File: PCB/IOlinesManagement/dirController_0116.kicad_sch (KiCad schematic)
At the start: 49 parts, among them K1 HK19F-DCxxV-SHC, K10 HK19F-DCxxV-SHC, K11 HK19F-DCxxV-SHC, K12 HK19F-DCxxV-SHC, K13 HK19F-DCxxV-SHC, K14 HK19F-DCxxV-SHC, K15 HK19F-DCxxV-SHC, K16 HK19F-DCxxV-SHC, K2 HK19F-DCxxV-SHC, K3 HK19F-DCxxV-SHC, K4 HK19F-DCxxV-SHC, K5 HK19F-DCxxV-SHC, K6 HK19F-DCxxV-SHC, K7 HK19F-DCxxV-SHC, K8 HK19F-DCxxV-SHC, K9 HK19F-DCxxV-SHC, Q1 BC337, Q10 BC337, Q11 BC337, Q12 BC337, Q13 BC337, Q14 BC337, Q15 BC337, Q16 BC337, Q2 BC337, Q3 BC337, Q4 BC337, Q5 BC337, Q6 BC337, Q7 BC337, Q8 BC337, Q9 BC337

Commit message: Duplicated components names fixed
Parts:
- renumbered K5 to K2, K2 to K3, K3 to K4, K4 to K5, Q2 to Q1, Q9 to Q10, Q10 to Q11, Q11 to Q12, Q14 to Q13, Q15 to Q14, Q16 to Q15, Q13 to Q16, Q1 to Q2, Q4 to Q3, Q3 to Q4, Q8 to Q5, Q5 to Q7, Q7 to Q8, Q12 to Q9, R9 to R10, R7 to R2, R2 to R3, R8 to R4, R4 to R7, R3 to R8, R10 to R9

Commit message: Fingerprints assignment
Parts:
- ExtPwr_1: footprint (none) -> Connector_PinHeader_2.54mm:PinHeader_2x09_P2.54mm_Vertical
- Q1, Q10, Q11, Q12, Q13, Q14, Q15, Q16, Q2, Q3, Q4, Q5, Q6, Q7, Q8, Q9: footprint Package_TO_SOT_THT:TO-92_Inline -> Package_TO_SOT_THT:TO-92_Inline_Wide
- R1, R10, R11, R12, R13, R14, R15, R16, R2, R3, R4, R5, R6, R7, R8, R9: footprint (none) -> Resistor_SMD:R_1206_3216Metric
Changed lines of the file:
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@@
 			)
 		)
-		(property "Footprint" "Package_TO_SOT_THT:TO-92_Inline"
+		(property "Footprint" "Package_TO_SOT_THT:TO-92_Inline_Wide"
 			(at 67.056 66.167 0)
 			(effects
@@
 			)
 		)
-		(property "Footprint" "Package_TO_SOT_THT:TO-92_Inline"
+		(property "Footprint" "Package_TO_SOT_THT:TO-92_Inline_Wide"
 			(at 192.278 89.027 0)
 			(effects
@@
 			)
 		)
-		(property "Footprint" "Package_TO_SOT_THT:TO-92_Inline"
+		(property "Footprint" "Package_TO_SOT_THT:TO-92_Inline_Wide"
 			(at 128.016 104.521 0)
 			(effects
@@
 			)
 		)
-		(property "Footprint" "Package_TO_SOT_THT:TO-92_Inline"
+		(property "Footprint" "Package_TO_SOT_THT:TO-92_Inline_Wide"
 			(at 67.056 104.267 0)
 			(effects
@@
 			)
 		)
-		(property "Footprint" "Package_TO_SOT_THT:TO-92_Inline"
+		(property "Footprint" "Package_TO_SOT_THT:TO-92_Inline_Wide"
 			(at 128.524 67.437 0)
 			(effects
@@
 			)
 		)
-		(property "Footprint" "Package_TO_SOT_THT:TO-92_Inline"
+		(property "Footprint" "Package_TO_SOT_THT:TO-92_Inline_Wide"
 			(at 129.032 141.605 0)
 			(effects
@@
 			)
 		)
-		(property "Footprint" ""
+		(property "Footprint" "Resistor_SMD:R_1206_3216Metric"
 			(at 160.528 149.098 90)
 			(effects
@@
 			)
 		)
-		(property "Footprint" "Package_TO_SOT_THT:TO-92_Inline"
+		(property "Footprint" "Package_TO_SOT_THT:TO-92_Inline_Wide"
 			(at 192.278 50.927 0)
 			(effects
@@
 			)
 		)
-		(property "Footprint" ""
+		(property "Footprint" "Resistor_SMD:R_1206_3216Metric"
 			(at 223.774 122.682 90)
 			(effects
@@
 			)
 		)
-		(property "Footprint" "Package_TO_SOT_THT:TO-92_Inline"
+		(property "Footprint" "Package_TO_SOT_THT:TO-92_Inline_Wide"
 			(at 67.31 178.689 0)
 			(effects
@@
 			)
 		)
-		(property "Footprint" "Package_TO_SOT_THT:TO-92_Inline"
+		(property "Footprint" "Package_TO_SOT_THT:TO-92_Inline_Wide"
 			(at 160.401 171.704 0)
 			(effects
@@
 			)
 		)
-		(property "Footprint" "Package_TO_SOT_THT:TO-92_Inline"
+		(property "Footprint" "Package_TO_SOT_THT:TO-92_Inline_Wide"
 			(at 254.254 126.365 0)
 			(effects
@@
 			)
 		)
-		(property "Footprint" ""
+		(property "Footprint" "Resistor_SMD:R_1206_3216Metric"
 			(at 49.53 100.584 90)
 			(effects
@@
 			)
 		)
-		(property "Footprint" ""
+		(property "Footprint" "Resistor_SMD:R_1206_3216Metric"
 			(at 177.038 47.244 90)
 			(effects
@@
 			)
 		)
-		(property "Footprint" ""
+		(property "Footprint" "Resistor_SMD:R_1206_3216Metric"
 			(at 223.774 160.02 90)
 			(effects
@@
 			)
 		)
-		(property "Footprint" "Package_TO_SOT_THT:TO-92_Inline"
+		(property "Footprint" "Package_TO_SOT_THT:TO-92_Inline_Wide"
 			(at 67.31 141.097 0)
 			(effects
@@
 			)
 		)
-		(property "Footprint" ""
+		(property "Footprint" "Resistor_SMD:R_1206_3216Metric"
 			(at 49.784 175.006 90)
 			(effects
@@
 			)
 		)
-		(property "Footprint" ""
+		(property "Footprint" "Resistor_SMD:R_1206_3216Metric"
 			(at 52.324 137.414 90)
 			(effects
@@
 			)
 		)
-		(property "Footprint" ""
+		(property "Footprint" "Resistor_SMD:R_1206_3216Metric"
 			(at 222.504 48.514 90)
 			(effects
@@
 			)
 		)
-		(property "Footprint" "Package_TO_SOT_THT:TO-92_Inline"
+		(property "Footprint" "Package_TO_SOT_THT:TO-92_Inline_Wide"
 			(at 192.532 125.857 0)
 			(effects
@@
 			)
 		)
-		(property "Footprint" "Package_TO_SOT_THT:TO-92_Inline"
+		(property "Footprint" "Package_TO_SOT_THT:TO-92_Inline_Wide"
 			(at 253.238 89.281 0)
 			(effects
@@
 			)
 		)
-		(property "Footprint" "Package_TO_SOT_THT:TO-92_Inline"
+		(property "Footprint" "Package_TO_SOT_THT:TO-92_Inline_Wide"
 			(at 259.207 150.368 0)
 			(effects
@@
 			)
 		)
-		(property "Footprint" ""
+		(property "Footprint" "Resistor_SMD:R_1206_3216Metric"
 			(at 97.282 63.754 90)
 			(effects
@@
 			)
 		)
-		(property "Footprint" "Package_TO_SOT_THT:TO-92_Inline"
+		(property "Footprint" "Package_TO_SOT_THT:TO-92_Inline_Wide"
 			(at 127 178.943 0)
 			(effects
@@
 			)
 		)
-		(property "Footprint" "Package_TO_SOT_THT:TO-92_Inline"
+		(property "Footprint" "Package_TO_SOT_THT:TO-92_Inline_Wide"
 			(at 253.746 52.197 0)
 			(effects
@@
 			)
 		)
-		(property "Footprint" ""
+		(property "Footprint" "Resistor_SMD:R_1206_3216Metric"
 			(at 225.044 85.598 90)
 			(effects
@@
 			)
 		)
-		(property "Footprint" ""
+		(property "Footprint" "Resistor_SMD:R_1206_3216Metric"
 			(at 174.752 85.344 90)
 			(effects
@@
 			)
 		)
-		(property "Footprint" ""
+		(property "Footprint" "Connector_PinHeader_2.54mm:PinHeader_2x09_P2.54mm_Vertical"
 			(at 23.114 19.558 0)
 			(effects
@@
 			)
 		)
-		(property "Footprint" ""
+		(property "Footprint" "Resistor_SMD:R_1206_3216Metric"
 			(at 177.546 122.174 90)
 			(effects
@@
 			)
 		)
-		(property "Footprint" ""
+		(property "Footprint" "Resistor_SMD:R_1206_3216Metric"
 			(at 51.816 62.484 90)
 			(effects
@@
 			)
 		)
-		(property "Footprint" ""
+		(property "Footprint" "Resistor_SMD:R_1206_3216Metric"
 			(at 98.552 175.26 90)
 			(effects
@@
 			)
 		)
-		(property "Footprint" ""
+		(property "Footprint" "Resistor_SMD:R_1206_3216Metric"
 			(at 98.552 137.922 90)
 			(effects
@@
 			)
 		)
-		(property "Footprint" ""
+		(property "Footprint" "Resistor_SMD:R_1206_3216Metric"
 			(at 99.822 100.838 90)
 			(effects

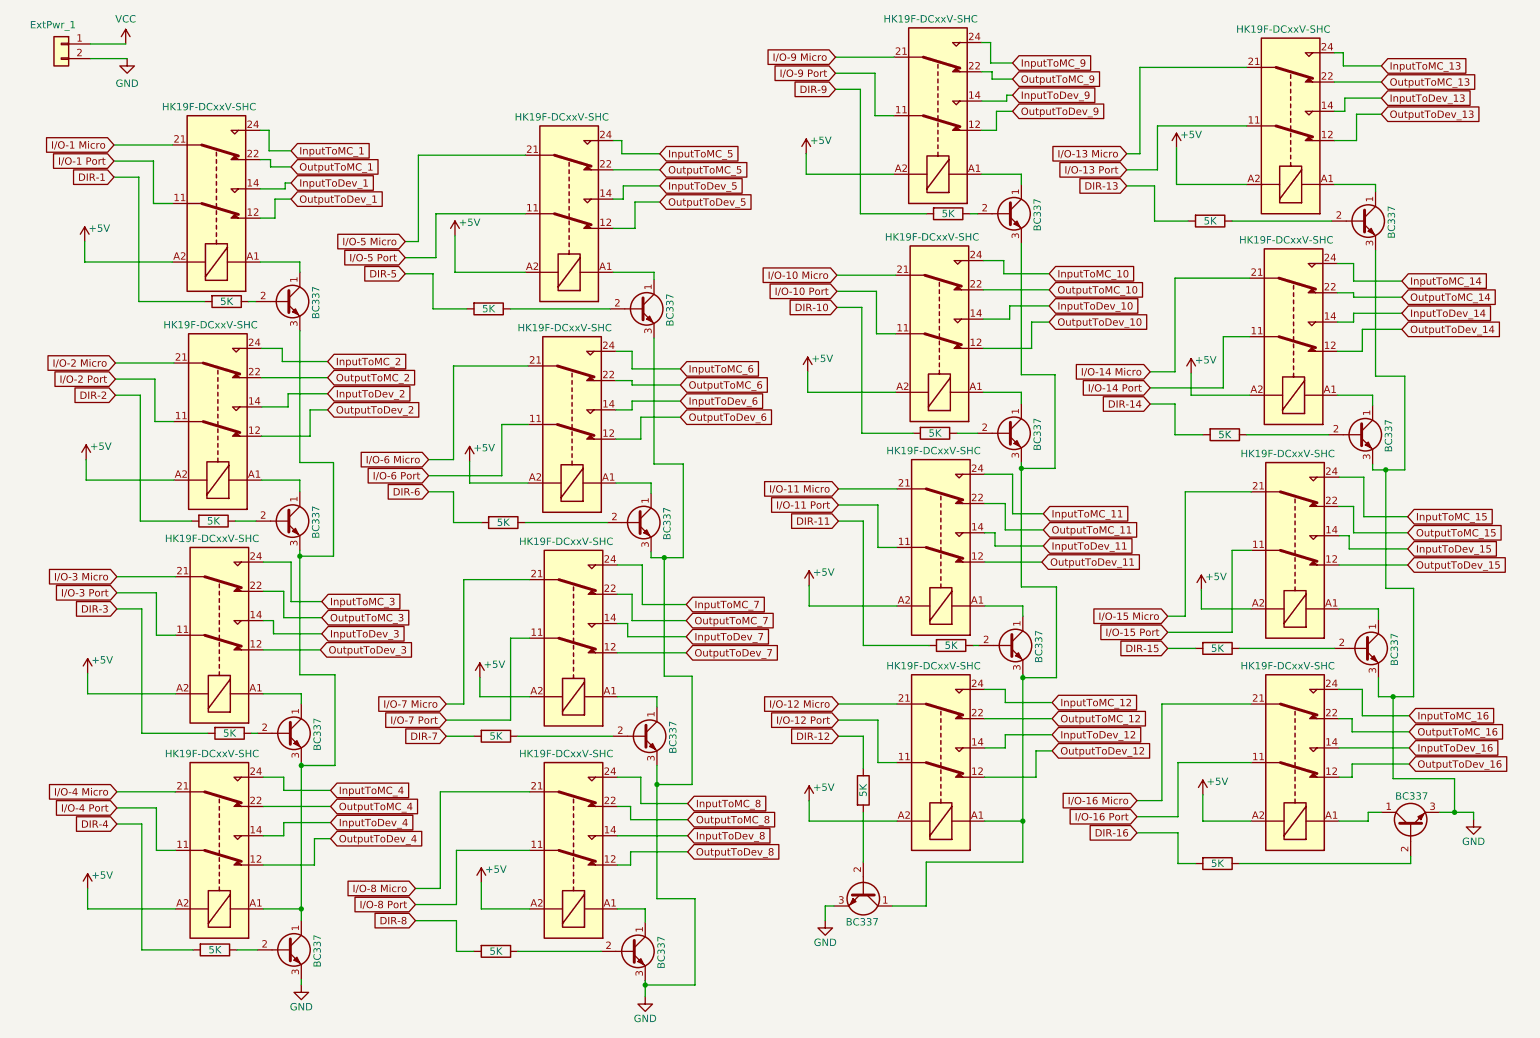
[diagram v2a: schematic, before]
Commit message: Component size reduction and fixes
- Some connection to GND has been fixed
- The biggest part of (THT) BC337 components has been replaced by (SMD) BC817
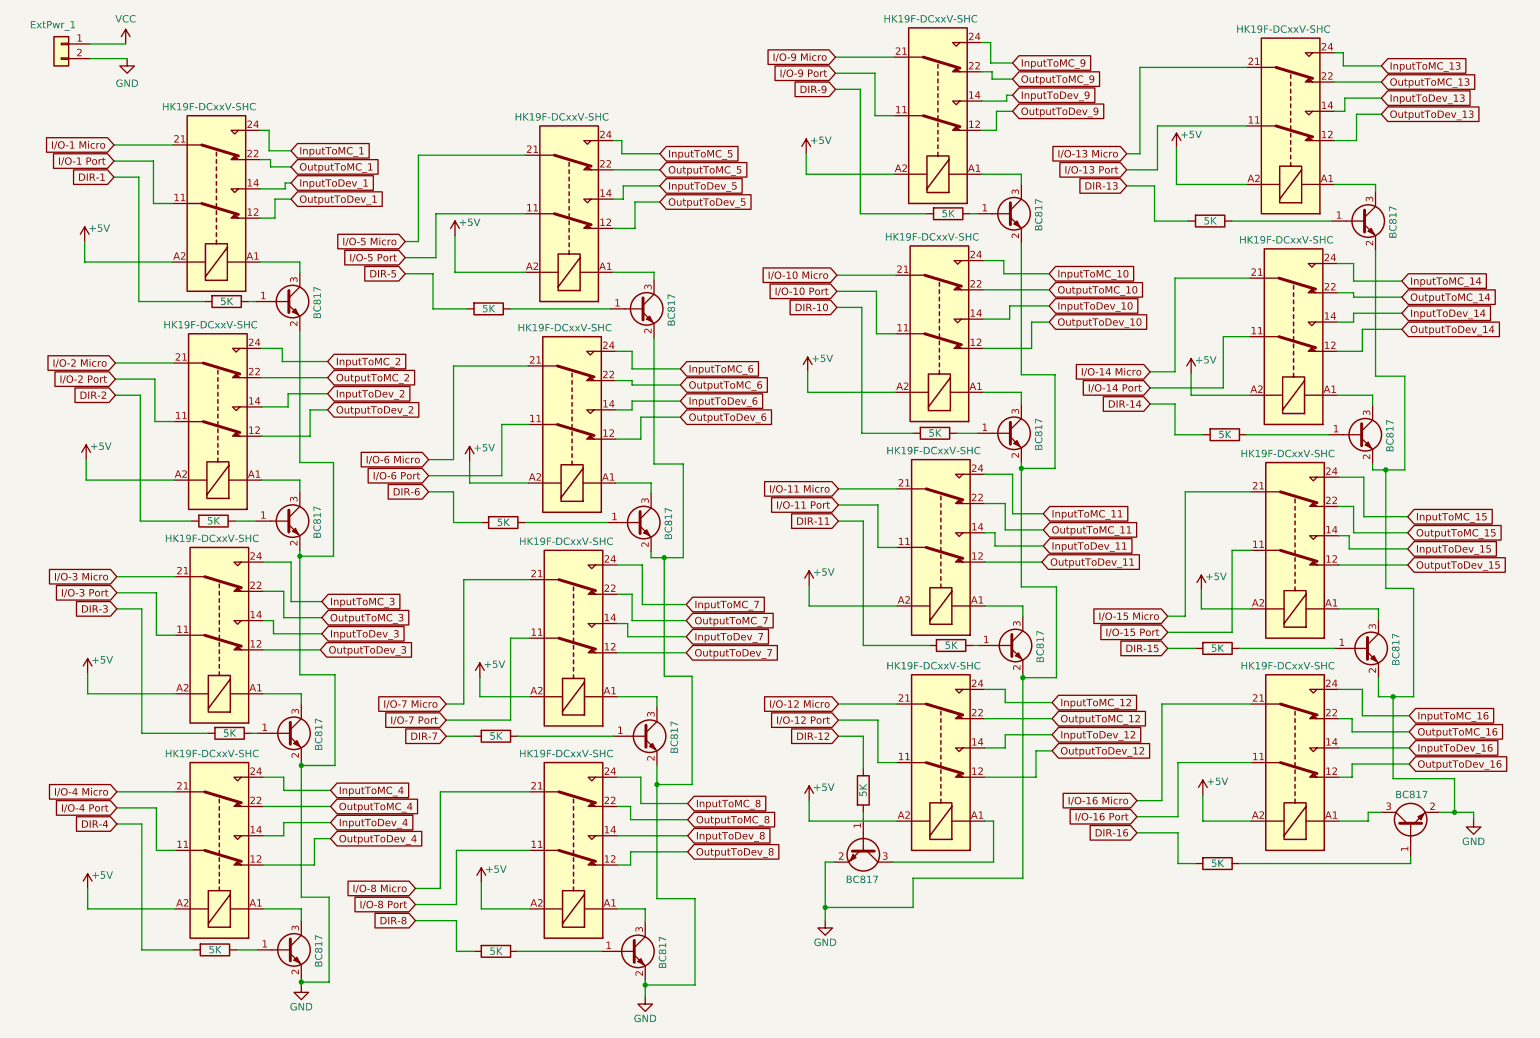
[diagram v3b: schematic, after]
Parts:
- removed Q1, Q10, Q11, Q12, Q13, Q14, Q15, Q16, Q2, Q3, Q4, Q5, Q6, Q7, Q8, Q9: BC337, Package_TO_SOT_THT:TO-92_Inline_Wide, symbol Transistor_BJT:BC337
- added Q1, Q10, Q11, Q12, Q13, Q14, Q15, Q16, Q2, Q3, Q4, Q5, Q6, Q7, Q8, Q9: BC817, Package_TO_SOT_SMD:SOT-23, symbol Transistor_BJT:BC817
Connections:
- net GND: now also Q1.2 (E), Q10.2 (E), Q11.2 (E), Q12.2 (E), Q13.2 (E), Q14.2 (E), Q15.2 (E), Q16.2 (E), Q2.2 (E), Q3.2 (E), Q4.2 (E), Q5.2 (E), Q6.2 (E), Q7.2 (E), Q8.2 (E), Q9.2 (E)
- net at K1.A1: now also Q1.3 (C)
- net at R3.1: now also Q1.1 (B)
- net at K4.A1: now also Q4.3 (C)
- net at K10.A1: now also Q10.3 (C)
- net at R10.1: now also Q10.1 (B)
- net at K12.A1: now also Q12.3 (C)
- net at K6.A1: now also Q6.3 (C)
- net at R8.1: now also Q6.1 (B)
- net at K2.A1: now also Q2.3 (C)
- net at R1.1: now also Q2.1 (B)
- net at K5.A1: now also Q5.3 (C)
- net at R5.1: now also Q5.1 (B)
- net at K16.A1: now also Q13.3 (C)
- net at K7.A1: now also Q7.3 (C)
- net at R6.1: now also Q7.1 (B)
- net at R9.2: now also Q12.1 (B)
- net at K13.A1: now also Q16.3 (C)
- net at K9.A1: now also Q9.3 (C)
- net at R11.1: now also Q9.1 (B)
- net at R14.1: now also Q14.1 (B)
- net at R2.1: now also Q4.1 (B)
- net at K15.A1: now also Q14.3 (C)
- net at R15.1: now also Q13.1 (B)
- net at K14.A1: now also Q15.3 (C)
- net at K8.A1: now also Q8.3 (C)
- net at K3.A1: now also Q3.3 (C)
- net at R4.1: now also Q3.1 (B)
- net at R13.1: now also Q16.1 (B)
- net at K11.A1: now also Q11.3 (C)
- net at R12.1: now also Q11.1 (B)
- net at R16.1: now also Q15.1 (B)
- net at R7.1: now also Q8.1 (B)

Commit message: Fixes
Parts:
- removed ExtPwr_1: Conn_01x02, Connector_PinHeader_2.54mm:PinHeader_2x09_P2.54mm_Vertical, symbol Connector_Generic:Conn_01x02
- renumbered Q9 to Q10, Q10 to Q11, Q11 to Q12, Q15 to Q13, Q16 to Q14, Q14 to Q15, Q13 to Q16, Q8 to Q5, Q5 to Q7, Q7 to Q8, Q12 to Q9
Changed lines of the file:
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@@
 	(wire
 		(pts
-			(xy 28.194 22.098) (xy 34.544 22.098)
-		)
-		(stroke
-			(width 0)
-			(type default)
-		)
-	)
-	(wire
-		(pts
 			(xy 162.306 139.7) (xy 162.306 145.288)
 		)
@@
 	(wire
 		(pts
-			(xy 28.194 19.558) (xy 34.29 19.558)
-		)
-		(stroke
-			(width 0)
-			(type default)
-		)
-	)
-	(wire
-		(pts
 			(xy 121.92 154.178) (xy 121.92 151.892)
 		)
@@
 	)
 	(symbol
-		(lib_id "power:VCC")
-		(at 34.29 19.558 0)
-		(unit 1)
-		(exclude_from_sim no)
-		(in_bom yes)
-		(on_board yes)
-		(dnp no)
-		(fields_autoplaced yes)
-		(property "Reference" "#PWR07"
-			(at 34.29 23.368 0)
-			(effects
-				(font
-					(size 1.27 1.27)
-				)
-				(hide yes)
-			)
-		)
-		(property "Value" "VCC"
-			(at 34.29 15.24 0)
-			(effects
-				(font
-					(size 1.27 1.27)
-				)
-			)
-		)
-		(property "Footprint" ""
-			(at 34.29 19.558 0)
-			(effects
-				(font
-					(size 1.27 1.27)
-				)
-				(hide yes)
-			)
-		)
-		(property "Datasheet" ""
-			(at 34.29 19.558 0)
-			(effects
-				(font
-					(size 1.27 1.27)
-				)
-				(hide yes)
-			)
-		)
-		(property "Description" "Power symbol creates a global label with name \"VCC\""
-			(at 34.29 19.558 0)
-			(effects
-				(font
-					(size 1.27 1.27)
-				)
-				(hide yes)
-			)
-		)
-		(pin "1"
-		)
-		(instances
-			(project ""
-				(path "/e1cfbeff-02ed-44cc-ae25-dce7e255cb28/07f29ec0-aae3-4d3e-a0d7-7681afcd2846"
-					(reference "#PWR07")
-					(unit 1)
-				)
-			)
-		)
-	)
-	(symbol
 		(lib_id "Transistor_BJT:BC817")
 		(at 187.198 49.022 0)
@@
 		(on_board yes)
 		(dnp no)
-		(property "Reference" "Q9"
+		(property "Reference" "Q10"
 			(at 192.532 47.7519 0)
 			(effects
@@
 			(project "main"
 				(path "/e1cfbeff-02ed-44cc-ae25-dce7e255cb28/07f29ec0-aae3-4d3e-a0d7-7681afcd2846"
-					(reference "Q9")
+					(reference "Q10")
 					(unit 1)
 				)
@@
 		(on_board yes)
 		(dnp no)
-		(property "Reference" "Q14"
+		(property "Reference" "Q15"
 			(at 254.508 123.1899 0)
 			(effects
@@
 			(project "main"
 				(path "/e1cfbeff-02ed-44cc-ae25-dce7e255cb28/07f29ec0-aae3-4d3e-a0d7-7681afcd2846"
-					(reference "Q14")
+					(reference "Q15")
 					(unit 1)
 				)
@@
 		(on_board yes)
 		(dnp no)
-		(property "Reference" "Q11"
+		(property "Reference" "Q12"
 			(at 192.786 122.6819 0)
 			(effects
@@
 			(project "main"
 				(path "/e1cfbeff-02ed-44cc-ae25-dce7e255cb28/07f29ec0-aae3-4d3e-a0d7-7681afcd2846"
-					(reference "Q11")
+					(reference "Q12")
 					(unit 1)
 				)
@@
 		(on_board yes)
 		(dnp no)
-		(property "Reference" "Q12"
+		(property "Reference" "Q9"
 			(at 163.5761 164.338 0)
 			(effects
@@
 			(project "main"
 				(path "/e1cfbeff-02ed-44cc-ae25-dce7e255cb28/07f29ec0-aae3-4d3e-a0d7-7681afcd2846"
-					(reference "Q12")
+					(reference "Q9")
 					(unit 1)
 				)
@@
 		(on_board yes)
 		(dnp no)
-		(property "Reference" "Q16"
+		(property "Reference" "Q14"
 			(at 254 49.0219 0)
 			(effects
@@
 			(project "main"
 				(path "/e1cfbeff-02ed-44cc-ae25-dce7e255cb28/07f29ec0-aae3-4d3e-a0d7-7681afcd2846"
-					(reference "Q16")
+					(reference "Q14")
 					(unit 1)
 				)
@@
 		(on_board yes)
 		(dnp no)
-		(property "Reference" "Q10"
+		(property "Reference" "Q11"
 			(at 192.532 85.8519 0)
 			(effects
@@
 			(project "main"
 				(path "/e1cfbeff-02ed-44cc-ae25-dce7e255cb28/07f29ec0-aae3-4d3e-a0d7-7681afcd2846"
-					(reference "Q10")
+					(reference "Q11")
 					(unit 1)
 				)
@@
 		(on_board yes)
 		(dnp no)
-		(property "Reference" "Q15"
+		(property "Reference" "Q13"
 			(at 253.492 86.1059 0)
 			(effects
@@
 			(project "main"
 				(path "/e1cfbeff-02ed-44cc-ae25-dce7e255cb28/07f29ec0-aae3-4d3e-a0d7-7681afcd2846"
-					(reference "Q15")
+					(reference "Q13")
 					(unit 1)
 				)
@@
 		(on_board yes)
 		(dnp no)
-		(property "Reference" "Q8"
+		(property "Reference" "Q5"
 			(at 127.254 175.7679 0)
 			(effects
@@
 			(project "main"
 				(path "/e1cfbeff-02ed-44cc-ae25-dce7e255cb28/07f29ec0-aae3-4d3e-a0d7-7681afcd2846"
-					(reference "Q8")
+					(reference "Q5")
 					(unit 1)
 				)
@@
 	)
 	(symbol
-		(lib_id "power:GND")
-		(at 34.544 22.098 0)
-		(unit 1)
-		(exclude_from_sim no)
-		(in_bom yes)
-		(on_board yes)
-		(dnp no)
-		(fields_autoplaced yes)
-		(property "Reference" "#PWR08"
-			(at 34.544 28.448 0)
-			(effects
-				(font
-					(size 1.27 1.27)
-				)
-				(hide yes)
-			)
-		)
-		(property "Value" "GND"
-			(at 34.544 26.416 0)
-			(effects
-				(font
-					(size 1.27 1.27)
-				)
-			)
-		)
-		(property "Footprint" ""
-			(at 34.544 22.098 0)
-			(effects
-				(font
-					(size 1.27 1.27)
-				)
-				(hide yes)
-			)
-		)
-		(property "Datasheet" ""
-			(at 34.544 22.098 0)
-			(effects
-				(font
-					(size 1.27 1.27)
-				)
-				(hide yes)
-			)
-		)
-		(property "Description" "Power symbol creates a global label with name \"GND\" , ground"
-			(at 34.544 22.098 0)
-			(effects
-				(font
-					(size 1.27 1.27)
-				)
-				(hide yes)
-			)
-		)
-		(pin "1"
-		)
-		(instances
-			(project ""
-				(path "/e1cfbeff-02ed-44cc-ae25-dce7e255cb28/07f29ec0-aae3-4d3e-a0d7-7681afcd2846"
-					(reference "#PWR08")
-					(unit 1)
-				)
-			)
-		)
-	)
-	(symbol
 		(lib_id "Device:R")
 		(at 97.282 65.532 270)
@@
 		(on_board yes)
 		(dnp no)
-		(property "Reference" "Q5"
+		(property "Reference" "Q7"
 			(at 128.778 64.2619 0)
 			(effects
@@
 			(project "main"
 				(path "/e1cfbeff-02ed-44cc-ae25-dce7e255cb28/07f29ec0-aae3-4d3e-a0d7-7681afcd2846"
-					(reference "Q5")
+					(reference "Q7")
 					(unit 1)
 				)
@@
 	)
 	(symbol
-		(lib_id "Connector_Generic:Conn_01x02")
-		(at 23.114 19.558 0)
-		(mirror y)
-		(unit 1)
-		(exclude_from_sim no)
-		(in_bom yes)
-		(on_board yes)
-		(dnp no)
-		(property "Reference" "ExtPwr_1"
-			(at 25.654 16.256 0)
-			(effects
-				(font
-					(size 1.27 1.27)
-				)
-				(justify left)
-			)
-		)
-		(property "Value" "Conn_01x02"
-			(at 20.828 22.0979 0)
-			(effects
-				(font
-					(size 1.27 1.27)
-				)
-				(justify left)
-				(hide yes)
-			)
-		)
-		(property "Footprint" "Connector_PinHeader_2.54mm:PinHeader_2x09_P2.54mm_Vertical"
-			(at 23.114 19.558 0)
-			(effects
-				(font
-					(size 1.27 1.27)
-				)
-				(hide yes)
-			)
-		)
-		(property "Datasheet" "~"
-			(at 23.114 19.558 0)
-			(effects
-				(font
-					(size 1.27 1.27)
-				)
-				(hide yes)
-			)
-		)
-		(property "Description" "Generic connector, single row, 01x02, script generated (kicad-library-utils/schlib/autogen/connector/)"
-			(at 23.114 19.558 0)
-			(effects
-				(font
-					(size 1.27 1.27)
-				)
-				(hide yes)
-			)
-		)
-		(pin "2"
-		)
-		(pin "1"
-		)
-		(instances
-			(project ""
-				(path "/e1cfbeff-02ed-44cc-ae25-dce7e255cb28/07f29ec0-aae3-4d3e-a0d7-7681afcd2846"
-					(reference "ExtPwr_1")
-					(unit 1)
-				)
-			)
-		)
-	)
-	(symbol
 		(lib_id "power:+5V")
 		(at 95.758 129.54 0)
@@
 		(on_board yes)
 		(dnp no)
-		(property "Reference" "Q13"
+		(property "Reference" "Q16"
 			(at 256.0319 150.114 0)
 			(effects
@@
 			(project "main"
 				(path "/e1cfbeff-02ed-44cc-ae25-dce7e255cb28/07f29ec0-aae3-4d3e-a0d7-7681afcd2846"
-					(reference "Q13")
+					(reference "Q16")
 					(unit 1)
 				)
@@
 		(on_board yes)
 		(dnp no)
-		(property "Reference" "Q7"
+		(property "Reference" "Q8"
 			(at 129.286 138.4299 0)
 			(effects
@@
 			(project "main"
 				(path "/e1cfbeff-02ed-44cc-ae25-dce7e255cb28/07f29ec0-aae3-4d3e-a0d7-7681afcd2846"
-					(reference "Q7")
+					(reference "Q8")
 					(unit 1)
 				)
